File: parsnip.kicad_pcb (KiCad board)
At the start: 4 copper layers, 60 x 130 mm, 446 parts, among them J1 SPI BUS, J10 SOLAR, J11 SMA-KE-347-H13.5-1.6, J12 U.FL, J13 SMA-KE-347-H13.5-1.6, J14 GPIO_Expander, J15 LED 5V, J2 I2C3, J3 I2C1, J4 I2C2, J5 e-Ink Display Connector, J6 UART0, J7 USB4105-GF-A-060, J8 PD_I2C DEBUG, J9 BAT_PORT, Q1 CSD23280F3, Q10 SI2308, Q11 CSD17577Q3A, Q12 AO3401A, Q13 BSS138, Q14 2N7002, Q15 2N7002, Q16 TPN2R203NC, Q2 CSD15380F3, Q3 CSD23280F3, Q4 CSD15380F3, Q5 AON7544, Q6 AON7544, Q7 CSD18512Q5B, Q8 CSD18512Q5B, Q9 SI2308, SW1 ESP_RESET, SW2 BOOT, SW3 POWER/RESET, SW4 RESET_GNSS, SW5 SAFEBOOT_GNSS, U1 ESP32-S3-WROOM-1-N16R8, U10 TPS7A2033PDBVR, U11 TPS259474LRPWR, U12 E22P-915M30S, U13 LM61460AASQRJRRQ1, U14 LM61460AASQRJRRQ1, U15 TPS259474ARPWR, U16 SN74LVC1G74, U17 TCAL9539RTWRQ1, U18 WS2816B, U19 SN74LV1T34DCK, U2 QMC6309, U20 WS2816B, U21 M24512-DFMC6TG, U3 TVS2200DRV, U4 TPD8S300A, U5 TPS25751DREFR, U7 MAX17320G22+, U8 BQ25798, U9 NEO-F10N, Y1 32.768kHz, Y2 SX1M4.000M10F30TNN

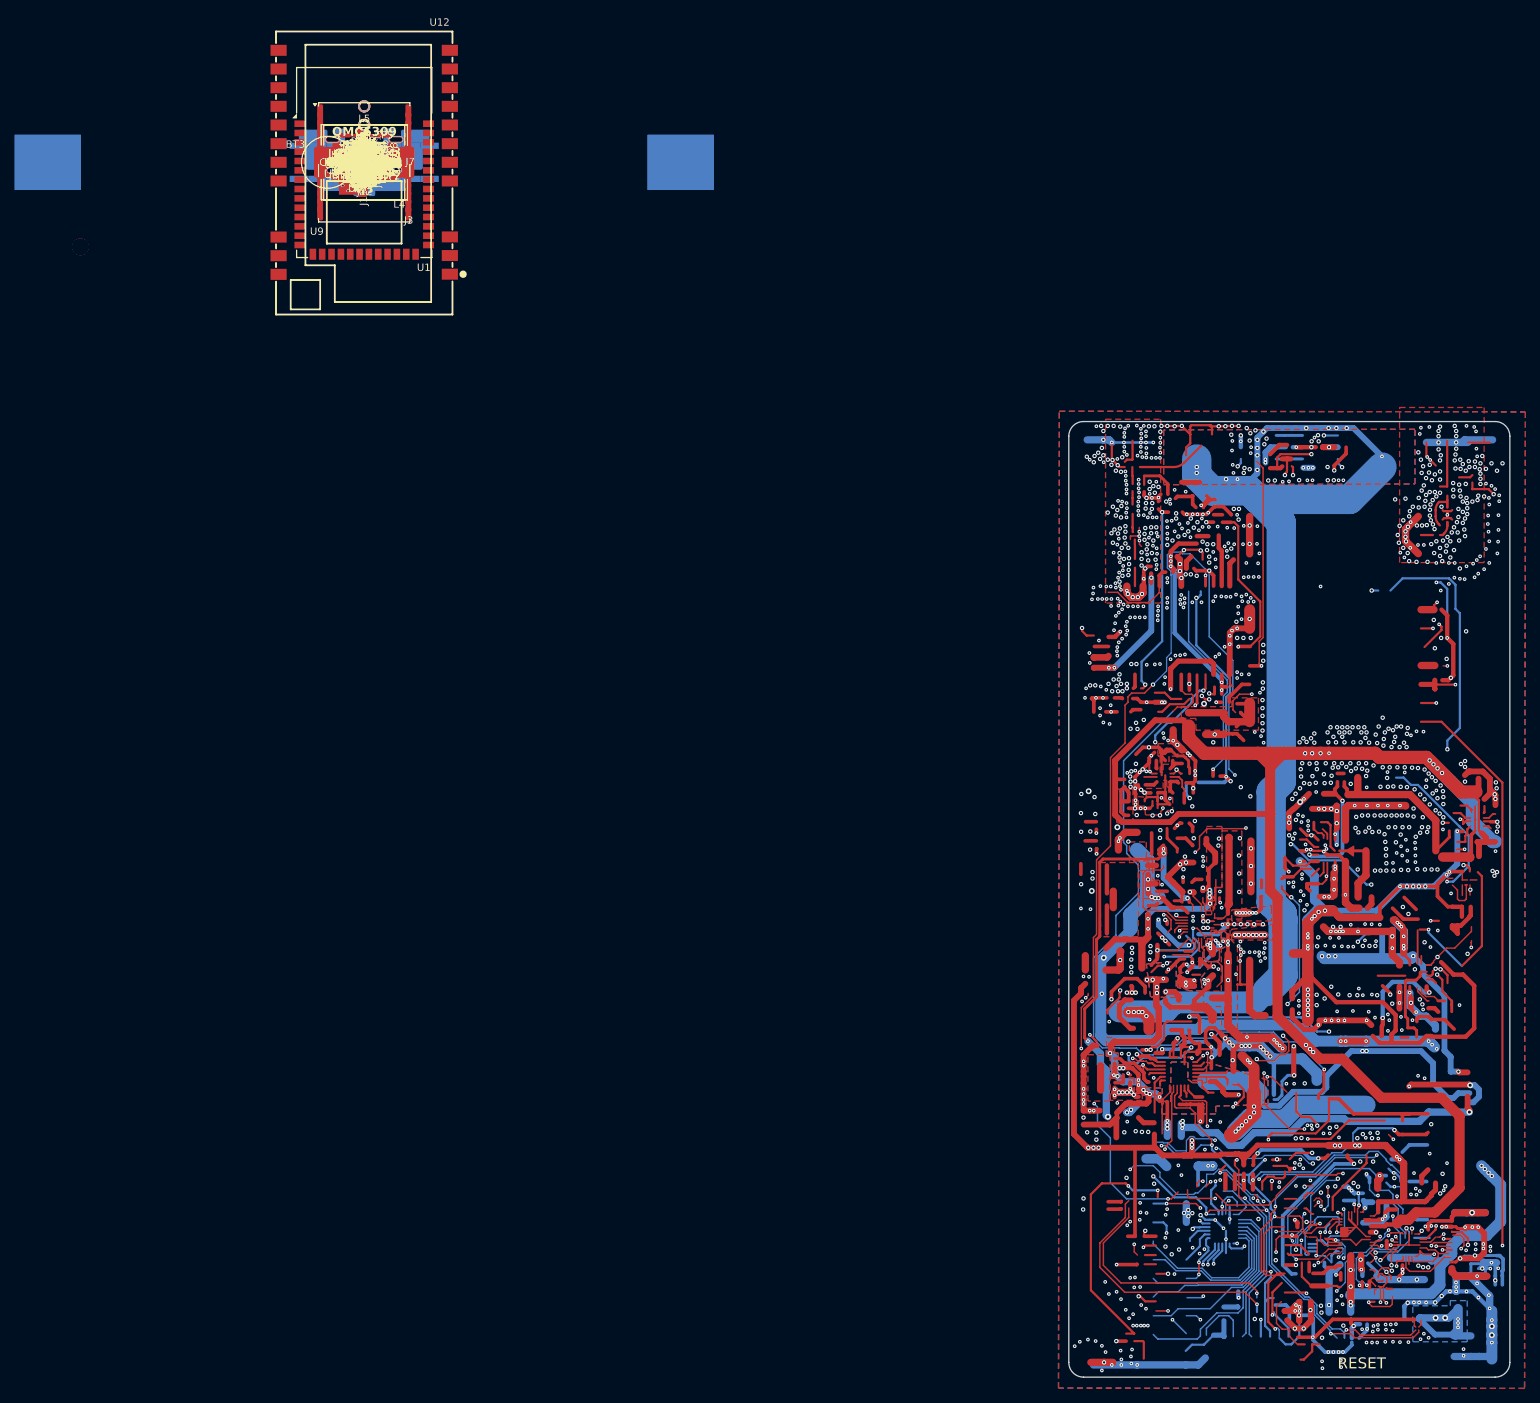
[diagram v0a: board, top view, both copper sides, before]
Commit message: routing and silkscreen improvements
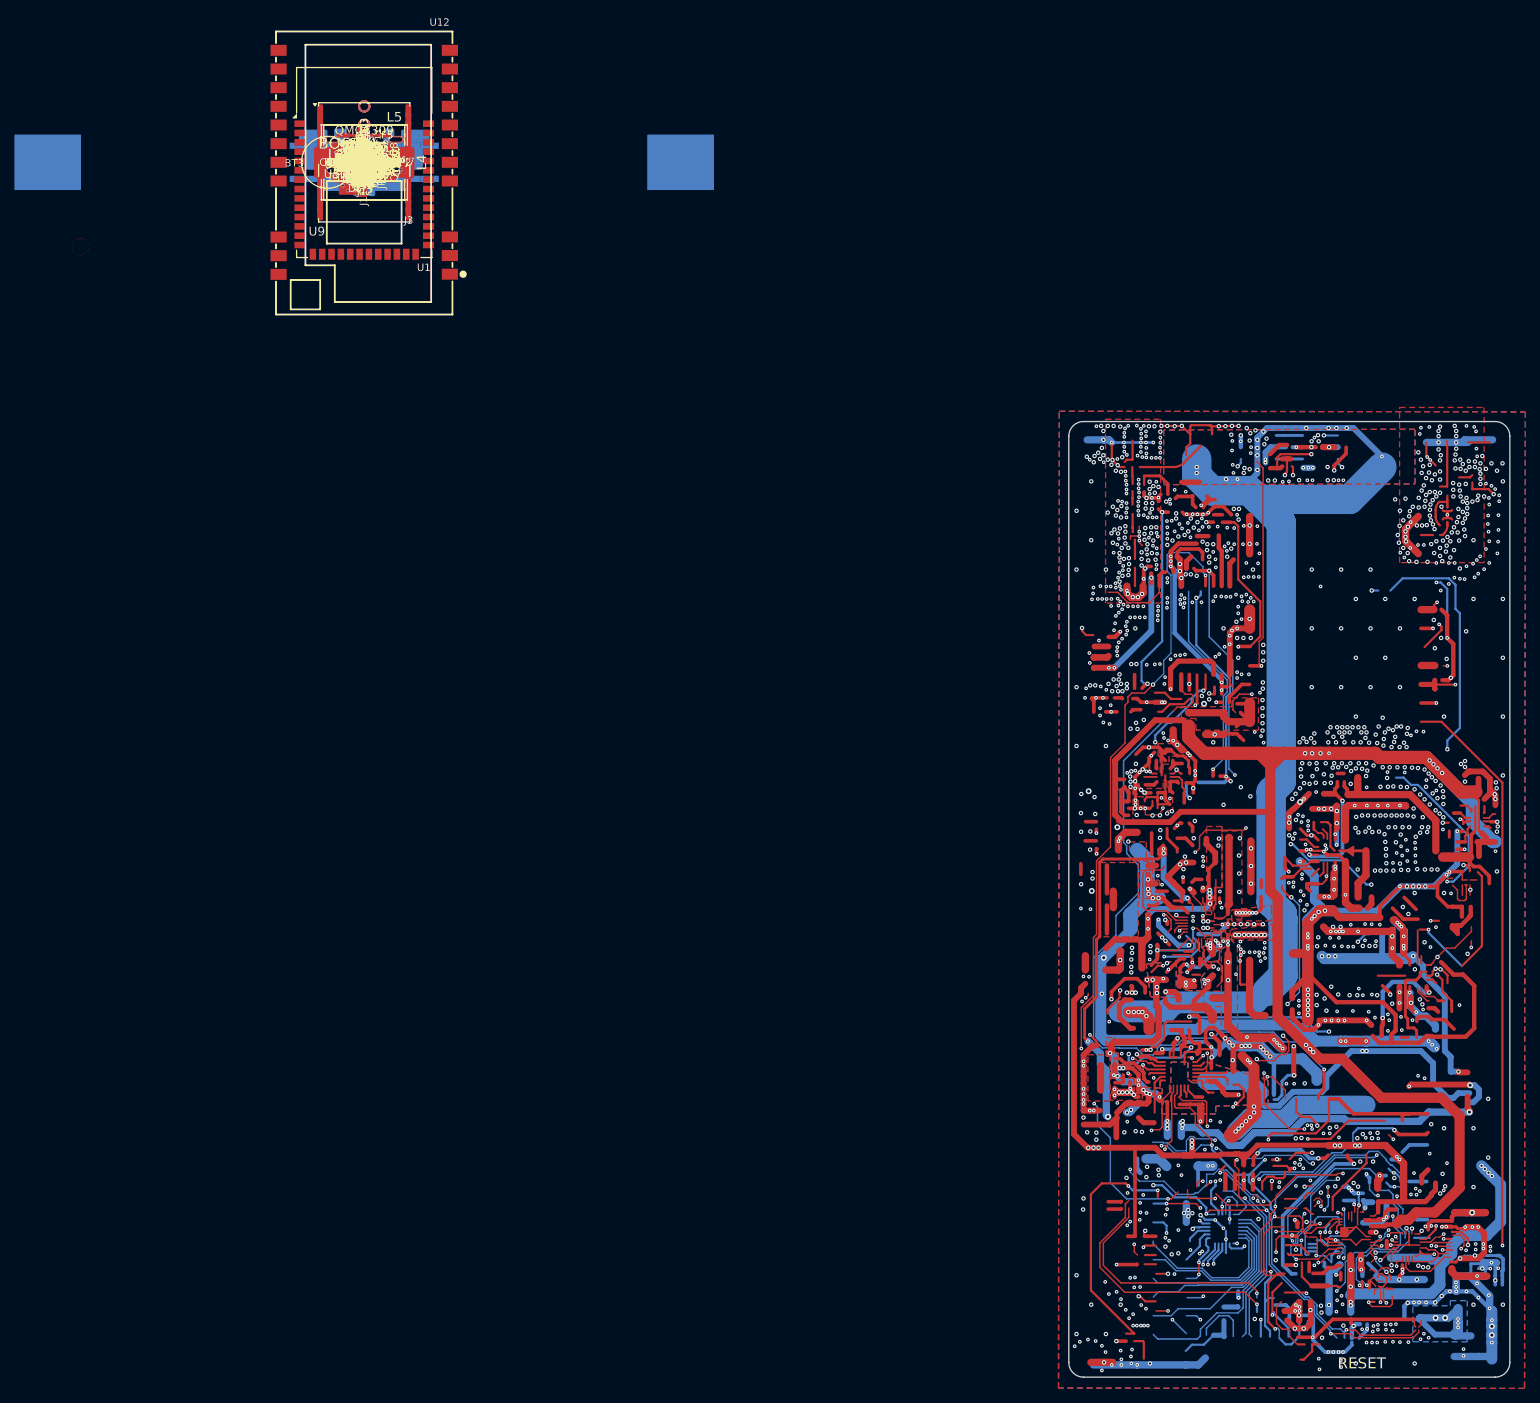
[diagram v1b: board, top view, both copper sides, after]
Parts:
- added C137: 10uF, Capacitor_SMD:C_0603_1608Metric, B.Cu at (0.00, 0.00)
- added C166, C167, C170, C171: 22uF, Capacitor_SMD:C_0603_1608Metric, F.Cu at (0.00, 0.00)
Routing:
- net I2C_HOST_IRQ: track 40.5 -> 71.5 mm, vias 4 -> 6
- net GND: track 639.4 -> 636.1 mm, vias 1265 -> 1320
- net /Root/Rails/5V_RAW: track 37.3 -> 39.8 mm
- net Net-(J15-Pin_1): track 3.25 -> 5.34 mm
- net +3V3: track 595.2 -> 594.1 mm
- net /Root/GNSS/SCL/SPI_CLK: track 86.9 -> 87.7 mm
- net I2C_PMIC_IRQ: track 91.1 -> 90.5 mm
- net /Charger/REGN: track 14.4 -> 14.9 mm
